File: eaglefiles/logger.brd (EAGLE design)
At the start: 43.2 x 20 mm, 39 parts, among them K1 65100516121, Q2 IRLML9301, U1 MCP1640, U3 FT232RLSSOP

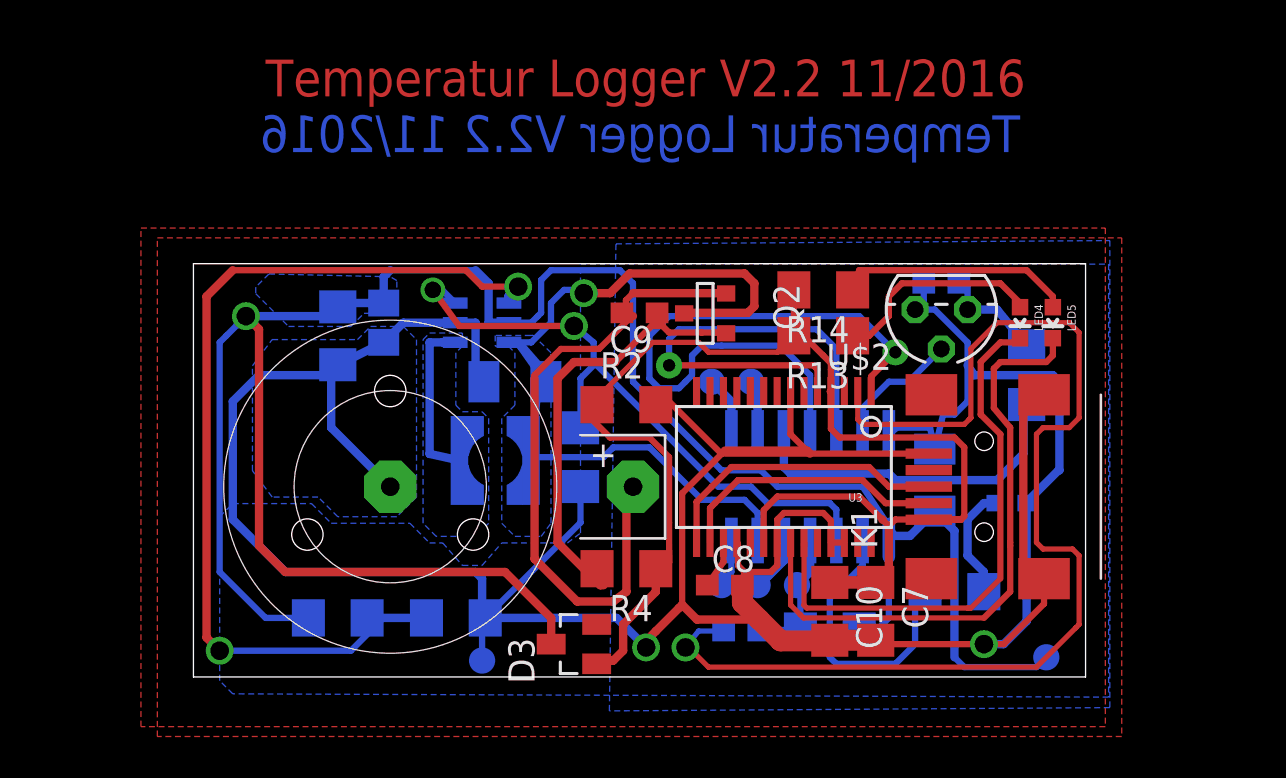
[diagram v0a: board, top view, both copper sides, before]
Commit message: Replaced mosfet by diode
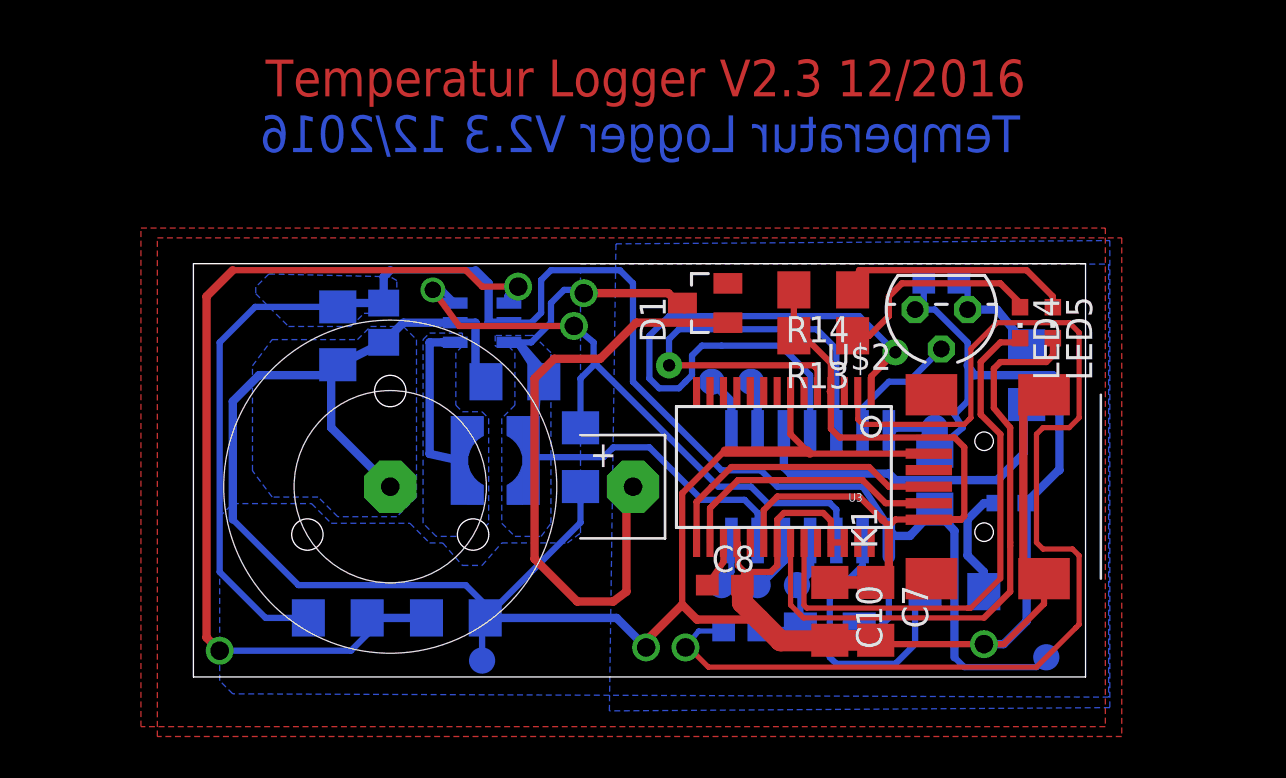
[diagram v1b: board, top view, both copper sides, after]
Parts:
- removed C9: 100nF, rcl:C0603
- removed D3: PMEG2010AET, diode:SOT23
- removed Q2: IRLML9301, 0liver:SOT-23
- removed R2: 100k, eagle-ltspice:R1206
- removed R4: 680, eagle-ltspice:R1206
- added D1: PMEG2010AET, diode:SOT23
- C2, C3: device rcl:C1206K -> rcl:C1206
- LED4, LED5: device SparkFun:LED-0603 -> led:CHIPLED_0603
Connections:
- removed net BATOFF: C9.1, Q2.3, R4.2
- net GND: no longer R2.2
- net N$6: now also D1.1; no longer C9.2, Q2.2
- net VCC: no longer D3.3
- net VSUPPLY: now also D1.3; no longer Q2.1
- net V_USB: no longer D3.1, R2.1, R4.1
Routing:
- net V_USB: track 66.9 -> 37.1 mm
- net VCC: track 113.5 -> 85.0 mm, vias 1 -> 0
- net BATOFF: track 21.9 -> 0.00 mm
- net VSUPPLY: track 42.3 -> 33.9 mm
- net GND: track 176.5 -> 172.7 mm
- net N$6: track 32.5 -> 30.3 mm
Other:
- board text added: "Temperatur Logger V2.3 12/2016"
- board text removed: "Temperatur Logger V2.2 11/2016"

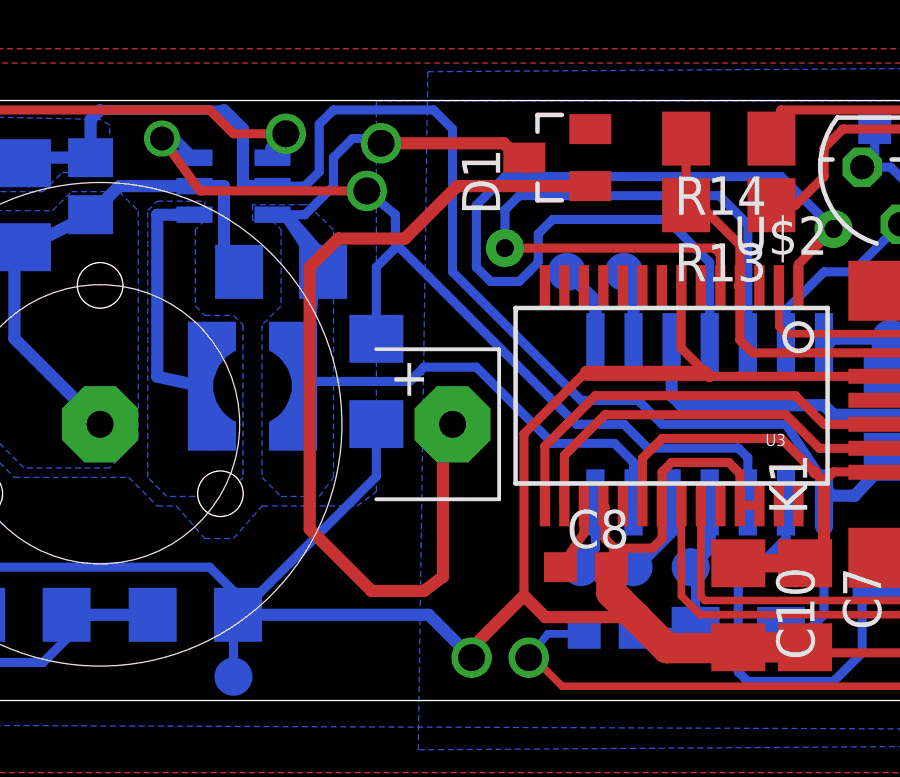
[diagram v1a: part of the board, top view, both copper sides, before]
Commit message: Replaced mosfet by diode
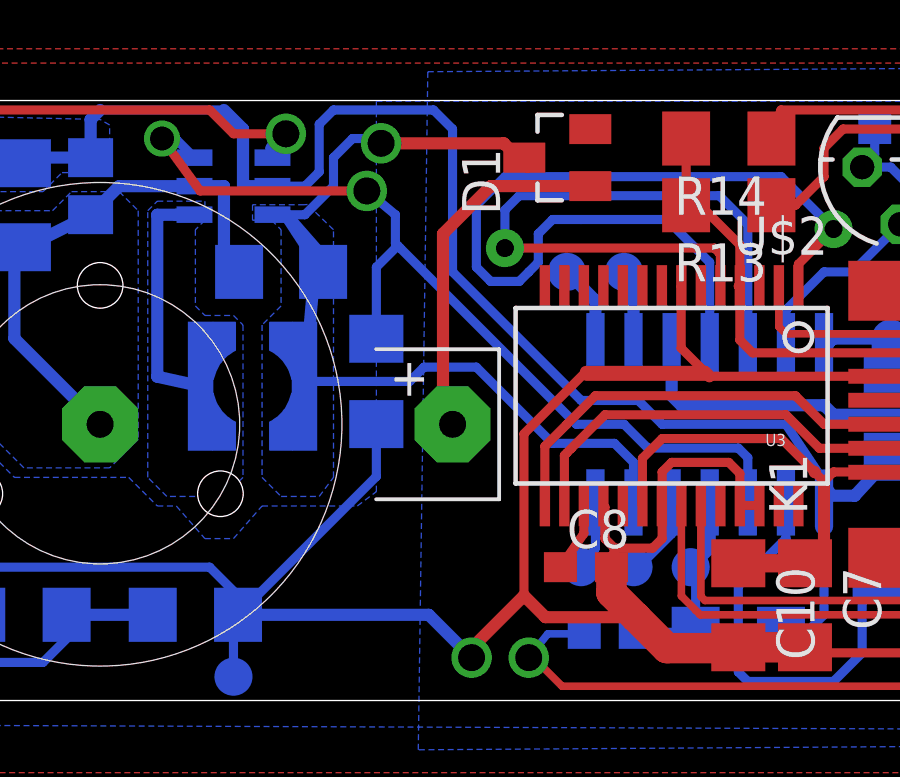
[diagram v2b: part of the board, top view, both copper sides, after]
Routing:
- net N$6: track 30.3 -> 12.1 mm
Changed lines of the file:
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@@
 <signal name="N$6">
 <contactref element="U$1" pad="P$2"/>
-<wire x1="16.51" y1="14.44625" x2="16.51" y2="5.715" width="0.4064" layer="1"/>
-<wire x1="16.51" y1="5.715" x2="18.57375" y2="3.65125" width="0.4064" layer="1"/>
-<wire x1="18.57375" y1="3.65125" x2="20.32" y2="3.65125" width="0.4064" layer="1"/>
-<wire x1="20.32" y1="3.65125" x2="20.955" y2="4.1275" width="0.4064" layer="1"/>
-<wire x1="20.955" y1="4.1275" x2="20.955" y2="9.36375" width="0.4064" layer="1"/>
-<wire x1="20.955" y1="9.36375" x2="21.275" y2="9.2075" width="0.4064" layer="1"/>
 <contactref element="D1" pad="1"/>
-<wire x1="16.51" y1="14.44625" x2="17.4625" y2="15.39875" width="0.4064" layer="1"/>
-<wire x1="17.4625" y1="15.39875" x2="19.685" y2="15.39875" width="0.4064" layer="1"/>
-<wire x1="19.685" y1="15.39875" x2="21.43375" y2="17.1475" width="0.4064" layer="1"/>
-<wire x1="21.43375" y1="17.1475" x2="25.865" y2="17.1475" width="0.4064" layer="1"/>
+<wire x1="25.865" y1="17.1475" x2="22.545" y2="17.1475" width="0.4064" layer="1"/>
+<wire x1="22.545" y1="17.1475" x2="20.955" y2="15.5575" width="0.4064" layer="1"/>
+<wire x1="20.955" y1="15.5575" x2="20.955" y2="9.5275" width="0.4064" layer="1"/>
+<wire x1="20.955" y1="9.5275" x2="21.275" y2="9.2075" width="0.4064" layer="1"/>
 </signal>
 <signal name="N$8">
